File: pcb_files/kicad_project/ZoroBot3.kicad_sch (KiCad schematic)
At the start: 117 parts, among them J2 MPU_CONNECTOR, Q5 NMOS, Q6 AON7423, U1 MPU-6500, Y1 Crystal

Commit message: Correlaciona toda la NetList, añade EdgeCuts y comienza el posicionamiento de componentes
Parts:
- removed J2: MPU_CONNECTOR, symbol Connector:Conn_01x06_Socket
- AD8418AWBZ_1, AD8418AWBZ_2: footprint (none) -> custom_footprints:SOP8
- AUX_CONN1: renamed from AUX_CONN; footprint (none) -> Connector_PinHeader_2.54mm:PinHeader_1x03_P2.54mm_Vertical
- BATT1: footprint (none) -> Connector_JST:JST_PH_B3B-PH-K_1x03_P2.00mm_Vertical
- BTN1, BTN2, BTN3: footprint Button_Switch_SMD:SW_Push_1P1T_NO_6x6mm_H9.5mm -> custom_footprints:Generic_SmallButton_6x3
- BTN_RST1: renamed from BTN_RST; footprint Button_Switch_SMD:SW_Push_1P1T_NO_6x6mm_H9.5mm -> custom_footprints:Generic_SmallButton_6x3
- C1, C10, C11, C12, C13, C14, C15, C16, C17, C18, C19, C2, C20, C21, C22, C3, C4, C6, C7, C9, CR1: footprint Capacitor_SMD:C_0805_2012Metric -> Capacitor_SMD:C_0402_1005Metric_Pad0.74x0.62mm_HandSolder
- C23: renamed from C49; footprint Capacitor_SMD:C_0805_2012Metric -> Capacitor_SMD:C_0402_1005Metric_Pad0.74x0.62mm_HandSolder
- C24: renamed from C50; footprint Capacitor_SMD:C_0805_2012Metric -> Capacitor_SMD:C_0402_1005Metric_Pad0.74x0.62mm_HandSolder
- C25: renamed from C30; footprint Capacitor_SMD:C_0805_2012Metric -> Capacitor_SMD:C_0402_1005Metric_Pad0.74x0.62mm_HandSolder
- C26: renamed from C28; footprint Capacitor_SMD:C_0805_2012Metric -> Capacitor_SMD:C_0402_1005Metric_Pad0.74x0.62mm_HandSolder
- C27: renamed from C29; footprint Capacitor_SMD:C_0805_2012Metric -> Capacitor_SMD:C_0402_1005Metric_Pad0.74x0.62mm_HandSolder
- C28: renamed from C26; value 22uF -> 10uF; footprint Capacitor_SMD:C_1206_3216Metric -> Capacitor_SMD:C_0402_1005Metric_Pad0.74x0.62mm_HandSolder
- C30: renamed from C32; value 22uF -> 10uF; footprint Capacitor_SMD:C_0805_2012Metric -> Capacitor_SMD:C_0402_1005Metric_Pad0.74x0.62mm_HandSolder
- CR3: renamed from CR7; footprint Capacitor_SMD:C_0805_2012Metric_Pad1.18x1.45mm_HandSolder -> Capacitor_SMD:C_0402_1005Metric_Pad0.74x0.62mm_HandSolder
- CR4: renamed from CR5; footprint Capacitor_SMD:C_0805_2012Metric -> Capacitor_SMD:C_0402_1005Metric_Pad0.74x0.62mm_HandSolder
- CR6: renamed from CR2; footprint Capacitor_SMD:C_0805_2012Metric_Pad1.18x1.45mm_HandSolder -> Capacitor_SMD:C_0402_1005Metric_Pad0.74x0.62mm_HandSolder
- CR7: renamed from CR6; footprint Capacitor_SMD:C_0805_2012Metric -> Capacitor_SMD:C_0402_1005Metric_Pad0.74x0.62mm_HandSolder
- D11: footprint LED_SMD:LED_0805_2012Metric -> LED_SMD:LED_0402_1005Metric_Pad0.77x0.64mm_HandSolder
- D12: renamed from D10; footprint LED_SMD:LED_0805_2012Metric -> LED_SMD:LED_0402_1005Metric_Pad0.77x0.64mm_HandSolder
- DATA_MPU1: renamed from DATA_MPU; footprint (none) -> custom_footprints:1x05 Pad
- DC-DC1: footprint custom_footprints:SOP8_with_gnd_pad -> Package_SO:Texas_HTSOP-8-1EP_3.9x4.9mm_P1.27mm_EP2.95x4.9mm_Mask2.4x3.1mm_ThermalVias
- ENC_D1: renamed from ENC_R1; footprint (none) -> custom_footprints:FujitoraBot2_PCBmain_Encoder
- ENC_I1: renamed from ENC_L1; footprint (none) -> custom_footprints:FujitoraBot2_PCBmain_Encoder
- IR_RECIVER1, SEN_FRONT_D1, SEN_FRONT_I1, SEN_PARED_D1, SEN_PARED_I1: footprint (none) -> custom_footprints:1x05 Pad
- Mot_D1, Mot_I1, Mot_S1: footprint (none) -> Connector_Hirose:Hirose_DF13-02P-1.25DSA_1x02_P1.25mm_Vertical
- PH1: footprint (none) -> Package_SO:SSOP-24_5.3x8.2mm_P0.65mm
- POWER_MPU1: renamed from POWER_MPU; footprint (none) -> custom_footprints:1x05 Pad
- POWER_SWITCH1: footprint libs sueltas:MSK12C2 -> custom_footprints:Generic_Swich_ONOFF
- Q1: renamed from Q5; footprint (none) -> Package_TO_SOT_SMD:SOT-23
- Q2: renamed from Q6; footprint (none) -> Package_DFN_QFN:DFN-8-1EP_3x3mm_P0.65mm_EP1.55x2.4mm
- R1: renamed from R2; footprint Resistor_SMD:R_0805_2012Metric -> Resistor_SMD:R_0402_1005Metric_Pad0.72x0.64mm_HandSolder
- R10: renamed from R41; footprint Resistor_SMD:R_0805_2012Metric -> Resistor_SMD:R_0402_1005Metric_Pad0.72x0.64mm_HandSolder
- R11: renamed from R1; footprint Resistor_SMD:R_0805_2012Metric -> Resistor_SMD:R_0402_1005Metric_Pad0.72x0.64mm_HandSolder
- R12: renamed from R45; footprint (none) -> Resistor_SMD:R_1210_3225Metric
- R13: renamed from R44; footprint (none) -> Resistor_SMD:R_1210_3225Metric
- R14: renamed from R10; footprint Resistor_SMD:R_0805_2012Metric -> Resistor_SMD:R_0402_1005Metric_Pad0.72x0.64mm_HandSolder
- R15: renamed from R11; footprint Resistor_SMD:R_0805_2012Metric -> Resistor_SMD:R_0402_1005Metric_Pad0.72x0.64mm_HandSolder
- R16: renamed from R12; footprint Resistor_SMD:R_0805_2012Metric -> Resistor_SMD:R_0402_1005Metric_Pad0.72x0.64mm_HandSolder
- R17, R6, R7, R8, R9: footprint Resistor_SMD:R_0805_2012Metric -> Resistor_SMD:R_0402_1005Metric_Pad0.72x0.64mm_HandSolder
- R18: renamed from R21; footprint Resistor_SMD:R_0805_2012Metric -> Resistor_SMD:R_0402_1005Metric_Pad0.72x0.64mm_HandSolder
- R19: renamed from R29; footprint Resistor_SMD:R_0805_2012Metric -> Resistor_SMD:R_0402_1005Metric_Pad0.72x0.64mm_HandSolder
- R2: renamed from R3; footprint Resistor_SMD:R_0805_2012Metric -> Resistor_SMD:R_0402_1005Metric_Pad0.72x0.64mm_HandSolder
- R20: renamed from R46; footprint Resistor_SMD:R_0805_2012Metric -> Resistor_SMD:R_0402_1005Metric_Pad0.72x0.64mm_HandSolder
- R21: renamed from R15; footprint Resistor_SMD:R_0805_2012Metric -> Resistor_SMD:R_0402_1005Metric_Pad0.72x0.64mm_HandSolder
- R22: renamed from R14; footprint Resistor_SMD:R_0805_2012Metric -> Resistor_SMD:R_0402_1005Metric_Pad0.72x0.64mm_HandSolder
- R23: renamed from R13; footprint Resistor_SMD:R_0805_2012Metric -> Resistor_SMD:R_0402_1005Metric_Pad0.72x0.64mm_HandSolder
- R24: renamed from R20; footprint Resistor_SMD:R_0805_2012Metric -> Resistor_SMD:R_0402_1005Metric_Pad0.72x0.64mm_HandSolder
- R25: renamed from R23; footprint Resistor_SMD:R_0805_2012Metric -> Resistor_SMD:R_0402_1005Metric_Pad0.72x0.64mm_HandSolder
- R26: renamed from R22; footprint Resistor_SMD:R_0805_2012Metric -> Resistor_SMD:R_0402_1005Metric_Pad0.72x0.64mm_HandSolder
- R27: renamed from R24; footprint Resistor_SMD:R_0805_2012Metric -> Resistor_SMD:R_0402_1005Metric_Pad0.72x0.64mm_HandSolder
- R28: renamed from R30; footprint Resistor_SMD:R_0805_2012Metric -> Resistor_SMD:R_0402_1005Metric_Pad0.72x0.64mm_HandSolder
- R3: renamed from R4; footprint Resistor_SMD:R_0805_2012Metric -> Resistor_SMD:R_0402_1005Metric_Pad0.72x0.64mm_HandSolder
- R4: renamed from R5; footprint Resistor_SMD:R_0805_2012Metric -> Resistor_SMD:R_0402_1005Metric_Pad0.72x0.64mm_HandSolder
- R5: renamed from R40; footprint Resistor_SMD:R_0805_2012Metric -> Resistor_SMD:R_0402_1005Metric_Pad0.72x0.64mm_HandSolder
- USB1: footprint (none) -> custom_footprints:USB-C ST-Link USART
- Y1: footprint Crystal:Crystal_SMD_5032-2Pin_5.0x3.2mm -> Crystal:Crystal_SMD_TXC_7M-4Pin_3.2x2.5mm
- renumbered C27 to C29, C33 to C31, CR3 to CR2, CR4 to CR5, D13 to D10, D14 to D13, D12 to D5, JP4 to JP2, L2 to L1, MIC5219 to MIC1, R16 to R29, R18 to R30, R19 to R31, D5 to RGB1
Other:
- moved on the sheet: AUX_CONN1, D1, D10, D2, D3, D4, D5, D6, D7, D8, D9, ENC_D1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

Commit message: Corrige errores de esquematico, crea las PCBs auxiliares, y posiciona todos los elementos para comenzar el ruteado.
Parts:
- removed JP1: SolderJumper_3_Open, Jumper:SolderJumper-3_P1.3mm_Open_RoundedPad1.0x1.5mm, symbol PCB_ZoroBot_v3-rescue:SolderJumper_3_Open-Jumper
- removed Y1: Crystal, Crystal:Crystal_SMD_TXC_7M-4Pin_3.2x2.5mm, symbol Device:Crystal
- added Y1: Crystal_GND24, Crystal:Crystal_SMD_TXC_7M-4Pin_3.2x2.5mm, symbol Device:Crystal_GND24
- C28: value 10uF -> 0.1uf
- C29: value 47uF -> 0.1uF; footprint Capacitor_SMD:C_0805_2012Metric -> Capacitor_SMD:C_0402_1005Metric_Pad0.74x0.62mm_HandSolder
- DATA_MPU1: footprint custom_footprints:1x05 Pad -> custom_footprints:ZoroBot3_Data_MPU
- ENC_D1, ENC_I1: footprint custom_footprints:FujitoraBot2_PCBmain_Encoder -> custom_footprints:ZoroBot3_PCBmain_Encoder
- IR_RECIVER1: footprint custom_footprints:1x05 Pad -> custom_footprints:IR_SENSOR_SMD_TSSP77038ETR
- Mot_D1, Mot_I1, Mot_S1: footprint Connector_Hirose:Hirose_DF13-02P-1.25DSA_1x02_P1.25mm_Vertical -> custom_footprints:Connector_motor_1.25_Hirose_DF13-02P-1.25DSA_1x02_P1.25mm_Vertical
- POWER_MPU1: footprint custom_footprints:1x05 Pad -> custom_footprints:ZoroBot3_Power_MPU
- SEN_FRONT_D1, SEN_FRONT_I1, SEN_PARED_D1, SEN_PARED_I1: footprint custom_footprints:1x05 Pad -> custom_footprints:ZoroBot3_Main_sensors
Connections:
- net +3V3: now also PH1.6 (A02)
- net GND: now also Y1.2, Y1.4
- net at C15.2, DEIXAME_QUE_PENSE_1.6 (PH1/OSC_OUT): now also Y1.1
- net at C13.2, DEIXAME_QUE_PENSE_1.5 (PH0/OSC_IN): now also Y1.3
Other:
- moved on the sheet: AD8418AWBZ_1, AD8418AWBZ_2, C13, C15

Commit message: Finaliza el diseño de la PCB de ZoroBot3 Rebuild y añade gerbers y BOM
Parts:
- removed C14, C16: 0.1uF, Capacitor_SMD:C_0402_1005Metric_Pad0.74x0.62mm_HandSolder, symbol Device:C
- added C41, C42, C43, C44, C45, C46, C47, C48, C49, C50, C51, C52: 10uF, Capacitor_SMD:C_0402_1005Metric_Pad0.74x0.62mm_HandSolder, symbol Device:C
- BATT1: footprint Connector_JST:JST_PH_B3B-PH-K_1x03_P2.00mm_Vertical -> Connector_JST:JST_XH_B3B-XH-A_1x03_P2.50mm_Vertical
- CR4, CR7: footprint Capacitor_SMD:C_0402_1005Metric_Pad0.74x0.62mm_HandSolder -> Capacitor_SMD:C_0603_1608Metric
- CR6: value 0.1uF -> 47uF; footprint Capacitor_SMD:C_0402_1005Metric_Pad0.74x0.62mm_HandSolder -> Capacitor_SMD:C_1206_3216Metric
- D13: footprint Diode_SMD:D_1206_3216Metric -> Diode_SMD:D_0805_2012Metric_Pad1.15x1.40mm_HandSolder
- R12, R13: value 0.100 -> 0.05; footprint Resistor_SMD:R_1210_3225Metric -> Resistor_SMD:R_2512_6332Metric
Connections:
- net +3V3: now also PH1.19 (STBY), PH1.20 (Vcc), C44.1, C45.1, C46.1, C52.1; no longer PH1.5 (A02), PH1.6 (A02)
- net +5V: now also C47.1, C48.1, C49.1, C50.1, C51.1
- net BATT: now also PH1.13 (VM2), PH1.14 (VM3), PH1.24 (VM1), C41.2, C42.2, C43.2; no longer PH1.1 (A01), PH1.11 (B01), PH1.12 (B01)
- net GND: now also PH1.10 (PGND2), PH1.18 (GND), PH1.3 (PGND1), PH1.4 (PGND1), PH1.9 (PGND2), C41.1, C42.1, C43.1, C44.2, C45.2, C46.2, C47.2, C48.2, C49.2, C50.2, C51.2, C52.2; no longer PH1.15 (PWMB), PH1.16 (BIN2), PH1.21 (AIN1), PH1.22 (AIN2), PH1.7 (B02)
- net MOT_D-: now also PH1.5 (A02), PH1.6 (A02); no longer PH1.19 (STBY), PH1.20 (Vcc)
- net MOT_D_A: now also PH1.22 (AIN2); no longer PH1.3 (PGND1)
- net MOT_D_B: now also PH1.21 (AIN1); no longer PH1.4 (PGND1)
- net MOT_D_PWM: now also PH1.23 (PWMA); no longer PH1.2 (A01)
- net MOT_I+: now also PH1.7 (B02), PH1.8 (B02); no longer AD8418AWBZ_2.8 (+IN), R13.1
- net MOT_I-: now also AD8418AWBZ_2.1 (-IN), R13.1; no longer PH1.17 (BIN1), PH1.18 (GND)
- net MOT_I_A: now also PH1.17 (BIN1); no longer PH1.8 (B02)
- net MOT_I_B: now also PH1.16 (BIN2); no longer PH1.9 (PGND2)
- net MOT_I_PWM: now also PH1.15 (PWMB); no longer PH1.10 (PGND2)
- net SHUNT_MD: now also PH1.1 (A01), PH1.2 (A01); no longer PH1.23 (PWMA), PH1.24 (VM1)
- net SHUNT_MI: now also AD8418AWBZ_2.8 (+IN), PH1.11 (B01), PH1.12 (B01); no longer AD8418AWBZ_2.1 (-IN), PH1.13 (VM2), PH1.14 (VM3)
- net at R27.1, R28.1: now also POWER_SWITCH1.1 (A); no longer POWER_SWITCH1.3 (C)
- net ENC_1_A renamed ENC_D_I
- net ENC_D_I: now also DEIXAME_QUE_PENSE_1.54 (PD2); no longer DEIXAME_QUE_PENSE_1.59 (PB7)
- net ENC_1_B renamed ENC_D_A
- net ENC_D_A: now also DEIXAME_QUE_PENSE_1.57 (PB5); no longer DEIXAME_QUE_PENSE_1.58 (PB6)
- net ENC_1_I renamed ENC_D_B
- net ENC_D_B: now also DEIXAME_QUE_PENSE_1.56 (PB4); no longer DEIXAME_QUE_PENSE_1.55 (PB3)
- net ENC_2_A renamed ENC_I_I
- net ENC_I_I: now also DEIXAME_QUE_PENSE_1.55 (PB3); no longer DEIXAME_QUE_PENSE_1.57 (PB5)
- net ENC_2_B renamed ENC_I_A
- net ENC_I_A: now also DEIXAME_QUE_PENSE_1.59 (PB7); no longer DEIXAME_QUE_PENSE_1.56 (PB4)
- net ENC_2_I renamed ENC_I_B
- net ENC_I_B: now also DEIXAME_QUE_PENSE_1.58 (PB6); no longer DEIXAME_QUE_PENSE_1.54 (PD2)
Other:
- moved on the sheet: BATT1, C10, C23, C24, C30, C31, C5, C6, C7, C8, C9, CR3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

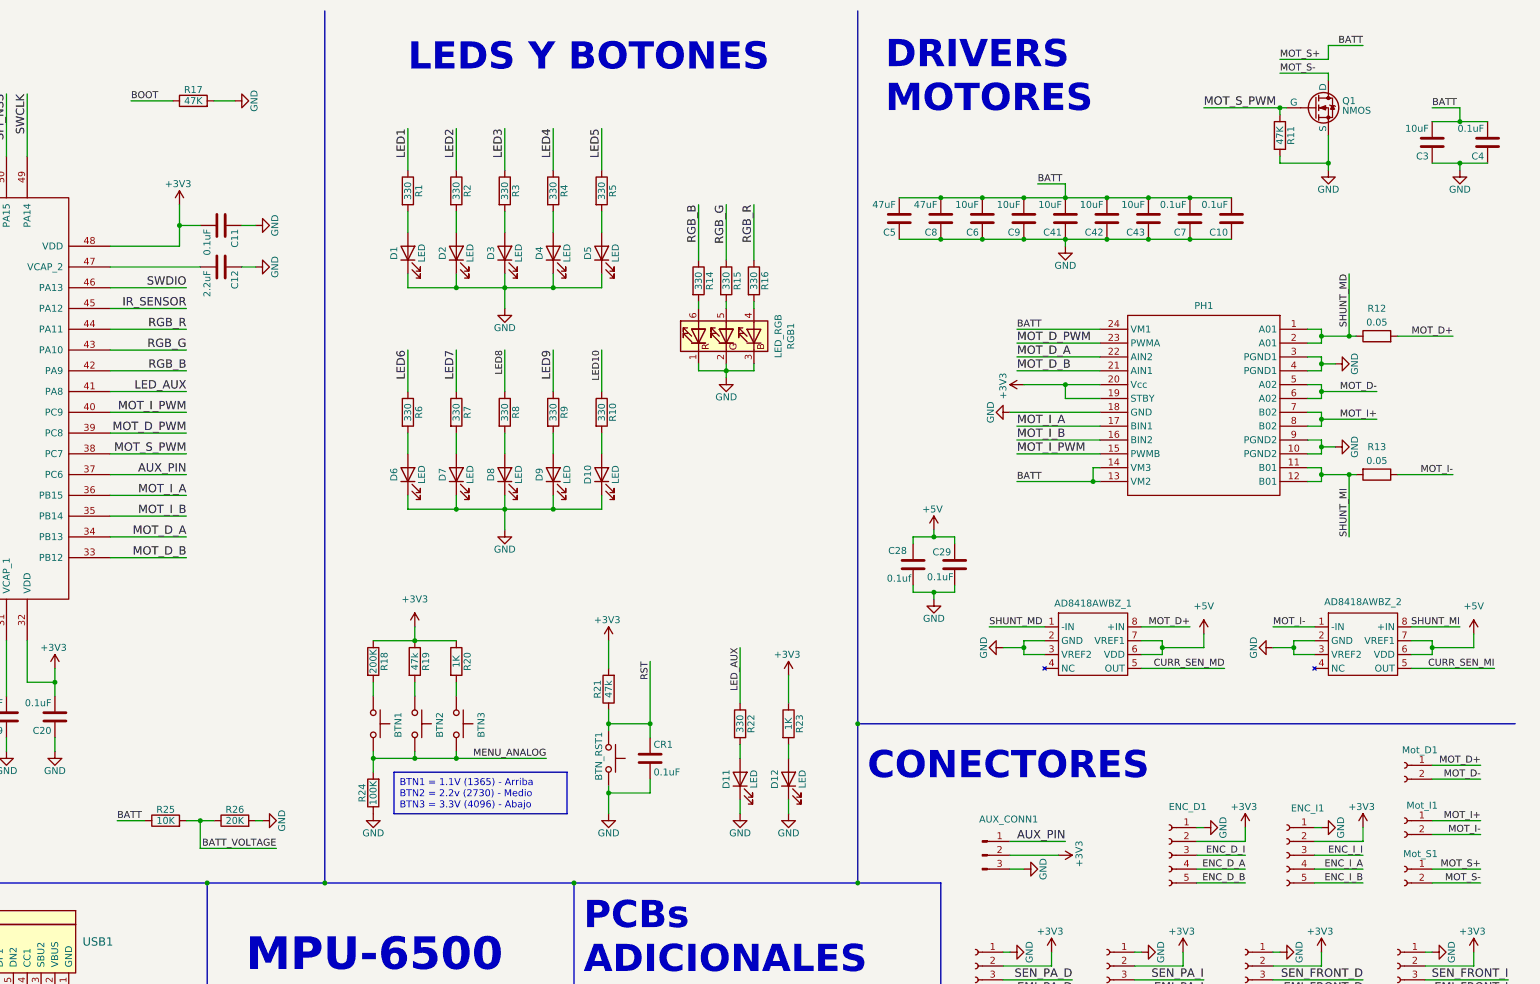
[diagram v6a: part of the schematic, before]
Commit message: Cambia el puente H al MP6551
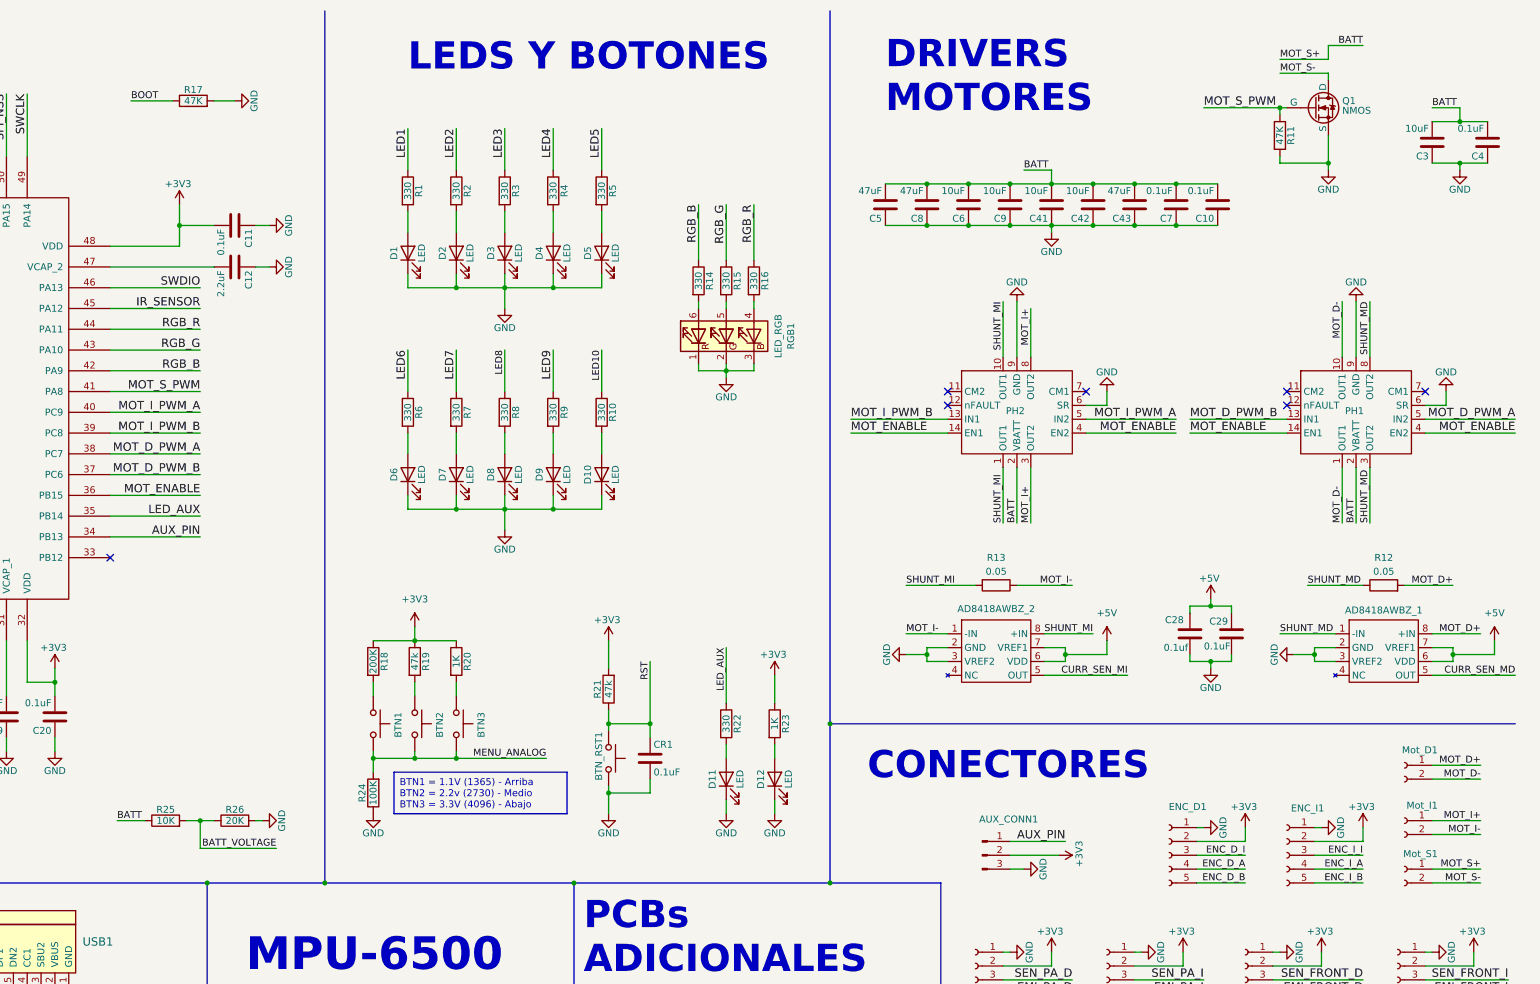
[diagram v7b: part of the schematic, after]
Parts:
- removed PH1: ~, Package_SO:SSOP-24_5.3x8.2mm_P0.65mm, symbol custom_symbols:TB6612FNG
- added PH1, PH2: ~, custom_footprints:PH-MP6551GQB-P, symbol custom_symbols:MP6551GQB-P
- C43: value 10uF -> 47uF; footprint Capacitor_SMD:C_0402_1005Metric_Pad0.74x0.62mm_HandSolder -> Capacitor_SMD:C_0805_2012Metric
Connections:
- net MOT_D_A is gone; now on net AUX_PIN: DEIXAME_QUE_PENSE_1.34 (PB13)
- net MOT_I_B is gone; now on net LED_AUX: DEIXAME_QUE_PENSE_1.35 (PB14)
- net AUX_PIN: no longer DEIXAME_QUE_PENSE_1.37 (PC6)
- net BATT: now also PH1.2 (VBATT), PH2.2 (VBATT)
- net GND: now also PH1.6 (SR), PH1.9 (GND), PH2.6 (SR), PH2.9 (GND)
- net LED_AUX: no longer DEIXAME_QUE_PENSE_1.41 (PA8)
- net MOT_D-: now also PH1.1 (OUT1), PH1.10 (OUT1)
- net MOT_I+: now also PH2.3 (OUT2), PH2.8 (OUT2)
- net MOT_S_PWM: now also DEIXAME_QUE_PENSE_1.41 (PA8); no longer DEIXAME_QUE_PENSE_1.38 (PC7)
- net SHUNT_MD: now also PH1.3 (OUT2), PH1.8 (OUT2)
- net SHUNT_MI: now also PH2.1 (OUT1), PH2.10 (OUT1)
- net MOT_D_B: no longer names the net of DEIXAME_QUE_PENSE_1.33 (PB12)
- net MOT_D_PWM renamed MOT_I_PWM_B
- net MOT_I_PWM_B: now also PH2.13 (IN1)
- net MOT_I_A renamed MOT_ENABLE
- net MOT_ENABLE: now also PH1.14 (EN1), PH1.4 (EN2), PH2.14 (EN1), PH2.4 (EN2)
- net MOT_I_PWM renamed MOT_I_PWM_A
- net MOT_I_PWM_A: now also PH2.5 (IN2)
- new net MOT_D_PWM_A: DEIXAME_QUE_PENSE_1.38 (PC7), PH1.5 (IN2)
- new net MOT_D_PWM_B: DEIXAME_QUE_PENSE_1.37 (PC6), PH1.13 (IN1)
- no-connect marks 7 -> 14
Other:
- moved on the sheet: AD8418AWBZ_1, AD8418AWBZ_2, C10, C11, C12, C28, C29, C41, C42, C43, C5, C6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
